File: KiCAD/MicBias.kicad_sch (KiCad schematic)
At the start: 24 parts

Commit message: Added a debug header
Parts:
- renumbered C68 to C62, C69 to C63, C66 to C64, C67 to C65, C64 to C66, C65 to C67, C62 to C68, C63 to C69, R51 to R41, R52 to R42, R49 to R43, R50 to R44, R55 to R45, R56 to R46, R53 to R47, R54 to R48, R43 to R49, R44 to R50, R41 to R51, R42 to R52, R47 to R53, R48 to R54, R45 to R55, R46 to R56
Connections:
- net IN1: now also C62.1; no longer C68.1
- net IN2: now also C63.1; no longer C69.1
- net IN3: now also C64.1; no longer C66.1
- net IN4: now also C65.1; no longer C67.1
- net IN5: now also C66.1; no longer C64.1
- net IN6: now also C67.1; no longer C65.1
- net IN7: now also C68.1; no longer C62.1
- net IN8: now also C69.1; no longer C63.1
- net OUT1: now also C62.2, R41.2, R45.1; no longer C68.2, R51.2, R55.1
- net OUT2: now also C63.2, R42.2, R46.1; no longer C69.2, R52.2, R56.1
- net OUT3: now also C64.2, R43.2, R47.1; no longer C66.2, R49.2, R53.1
- net OUT4: now also C65.2, R44.2, R48.1; no longer C67.2, R50.2, R54.1
- net OUT5: now also C66.2, R49.2, R53.1; no longer C64.2, R43.2, R47.1
- net OUT6: now also C67.2, R50.2, R54.1; no longer C65.2, R44.2, R48.1
- net OUT7: now also C68.2, R51.2, R55.1; no longer C62.2, R41.2, R45.1
- net OUT8: now also C69.2, R52.2, R56.1; no longer C63.2, R42.2, R46.1
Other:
- moved on the sheet: C62, C63, C64, C65, C66, C67, C68, C69, R41, R42, R43, R44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

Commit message: Added PA_Enable pull-down and moved the debug header
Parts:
- renumbered R41 to R42, R42 to R43, R43 to R44, R44 to R45, R45 to R46, R46 to R47, R47 to R48, R48 to R49, R49 to R50, R50 to R51, R51 to R52, R52 to R53, R53 to R54, R54 to R55, R55 to R56, R56 to R57

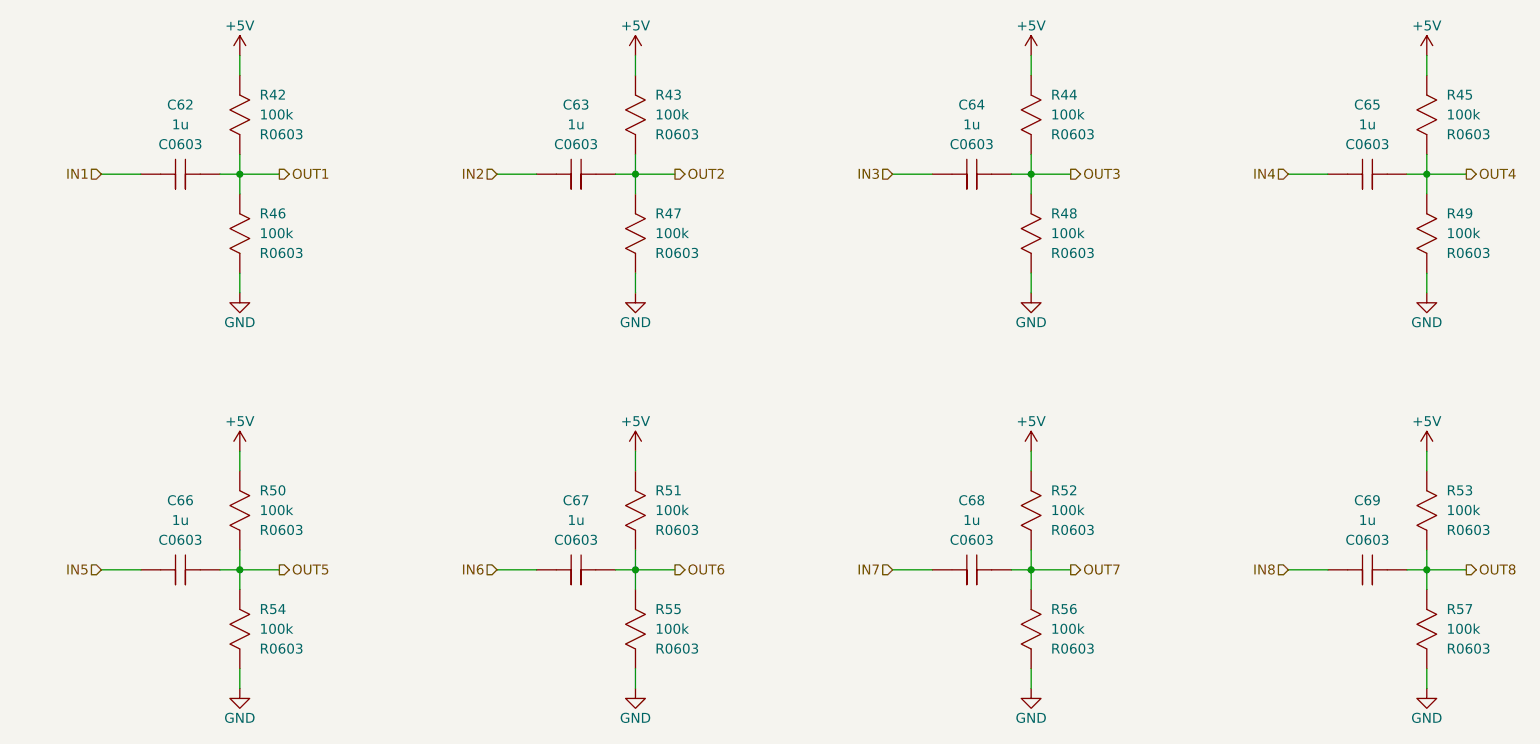
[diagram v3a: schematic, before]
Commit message: Moved the microphone RL to per-channel instead of per-mic
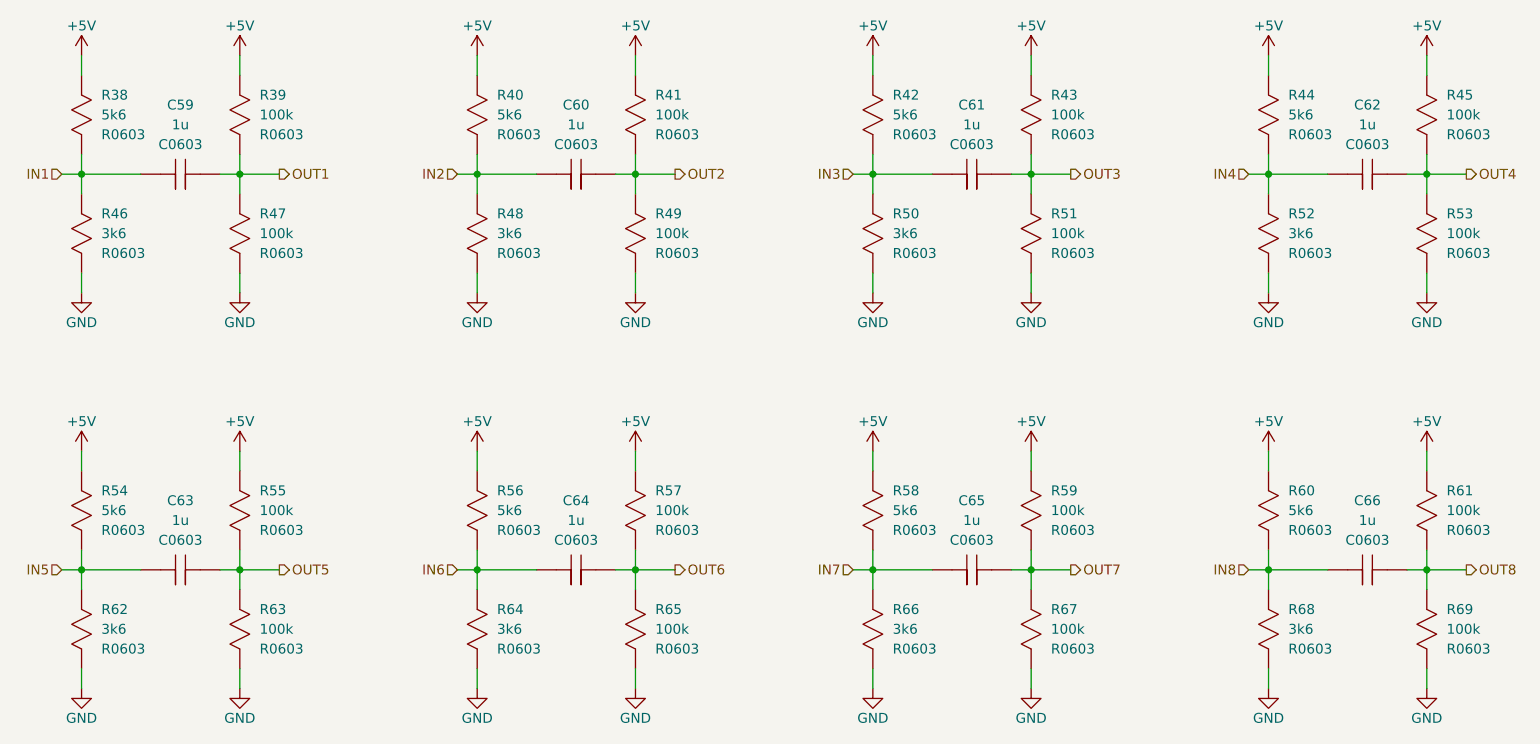
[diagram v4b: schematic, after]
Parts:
- added R38, R40, R42, R44, R54, R56, R58, R60: R0603_5k6, Resistor_SMD:R_0603_1608Metric, symbol Resistors0603:R0603_5k6
- added R46, R48, R50, R52, R62, R64, R66, R68: R0603_3k6, Resistor_SMD:R_0603_1608Metric, symbol Resistors0603:R0603_3k6
- renumbered C62 to C59, C63 to C60, C64 to C61, C65 to C62, C66 to C63, C67 to C64, C68 to C65, C69 to C66, R42 to R39, R43 to R41, R44 to R43, R46 to R47, R47 to R49, R48 to R51, R49 to R53, R50 to R55, R51 to R57, R52 to R59, R53 to R61, R54 to R63, R55 to R65, R56 to R67, R57 to R69
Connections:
- net +5V: now also R38.1, R40.1, R42.1, R44.1, R54.1, R56.1, R58.1, R60.1
- net GND: now also R46.2, R48.2, R50.2, R52.2, R62.2, R64.2, R66.2, R68.2
- net IN1: now also R38.2, R46.1
- net IN2: now also R40.2, R48.1
- net IN3: now also R42.2, R50.1
- net IN4: now also R44.2, R52.1
- net IN5: now also R54.2, R62.1
- net IN6: now also R56.2, R64.1
- net IN7: now also R58.2, R66.1
- net IN8: now also R60.2, R68.1

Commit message: Added title block and version text
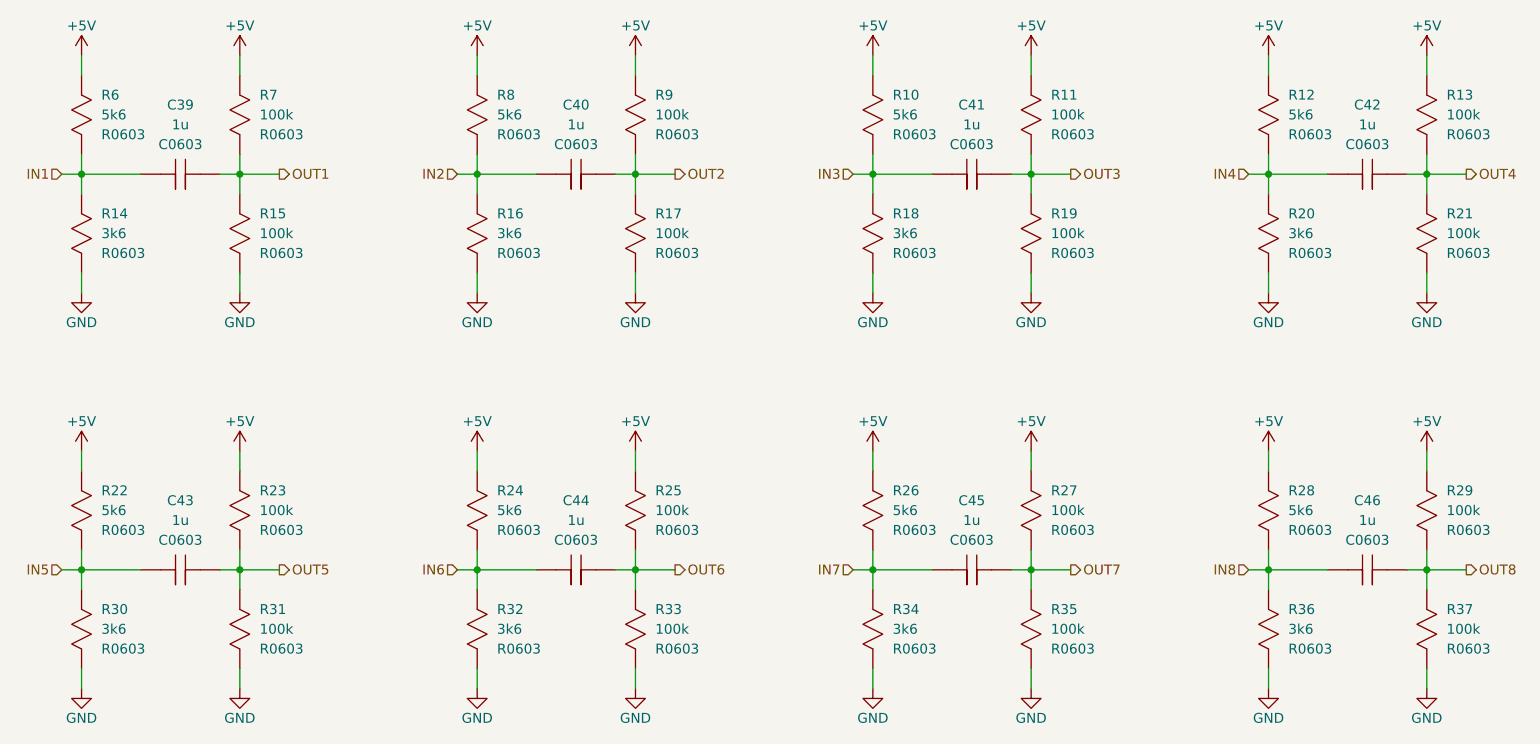
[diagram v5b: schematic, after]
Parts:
- renumbered C59 to C39, C60 to C40, C61 to C41, C62 to C42, C63 to C43, C64 to C44, C65 to C45, C66 to C46, R42 to R10, R43 to R11, R44 to R12, R45 to R13, R46 to R14, R47 to R15, R48 to R16, R49 to R17, R50 to R18, R51 to R19, R52 to R20, R53 to R21, R54 to R22, R55 to R23, R56 to R24, R57 to R25, R58 to R26, R59 to R27, R60 to R28, R61 to R29, R62 to R30, R63 to R31, R64 to R32, R65 to R33, R66 to R34, R67 to R35, R68 to R36, R69 to R37, R38 to R6, R39 to R7, R40 to R8, R41 to R9
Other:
- company: (none) -> University of Cape Town
- title: (none) -> Microphone Biassing

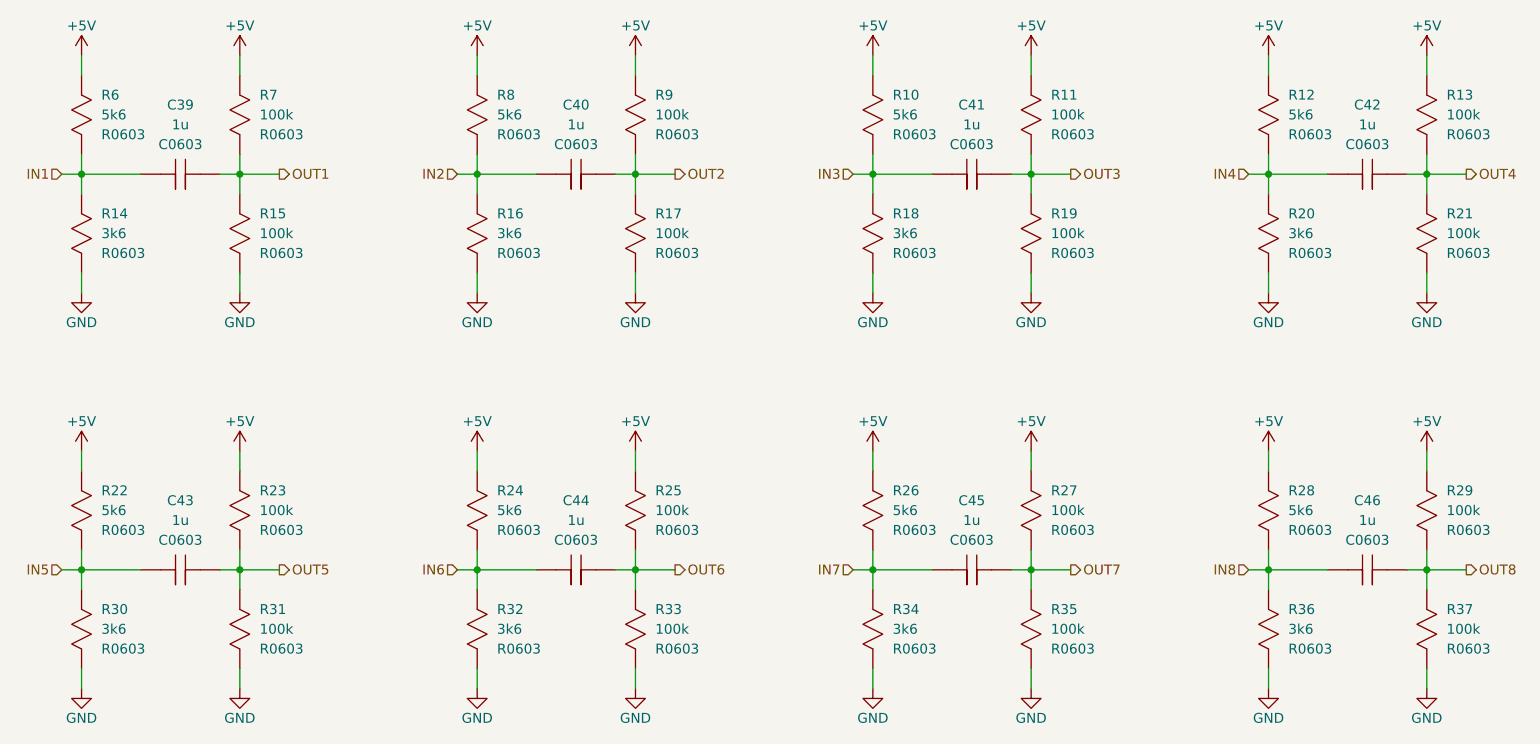
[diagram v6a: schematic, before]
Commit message: Final Updates:
- Mounting holes for an isolation shield
- 5V test-point to inject power
- Test signal input with resistor ladder
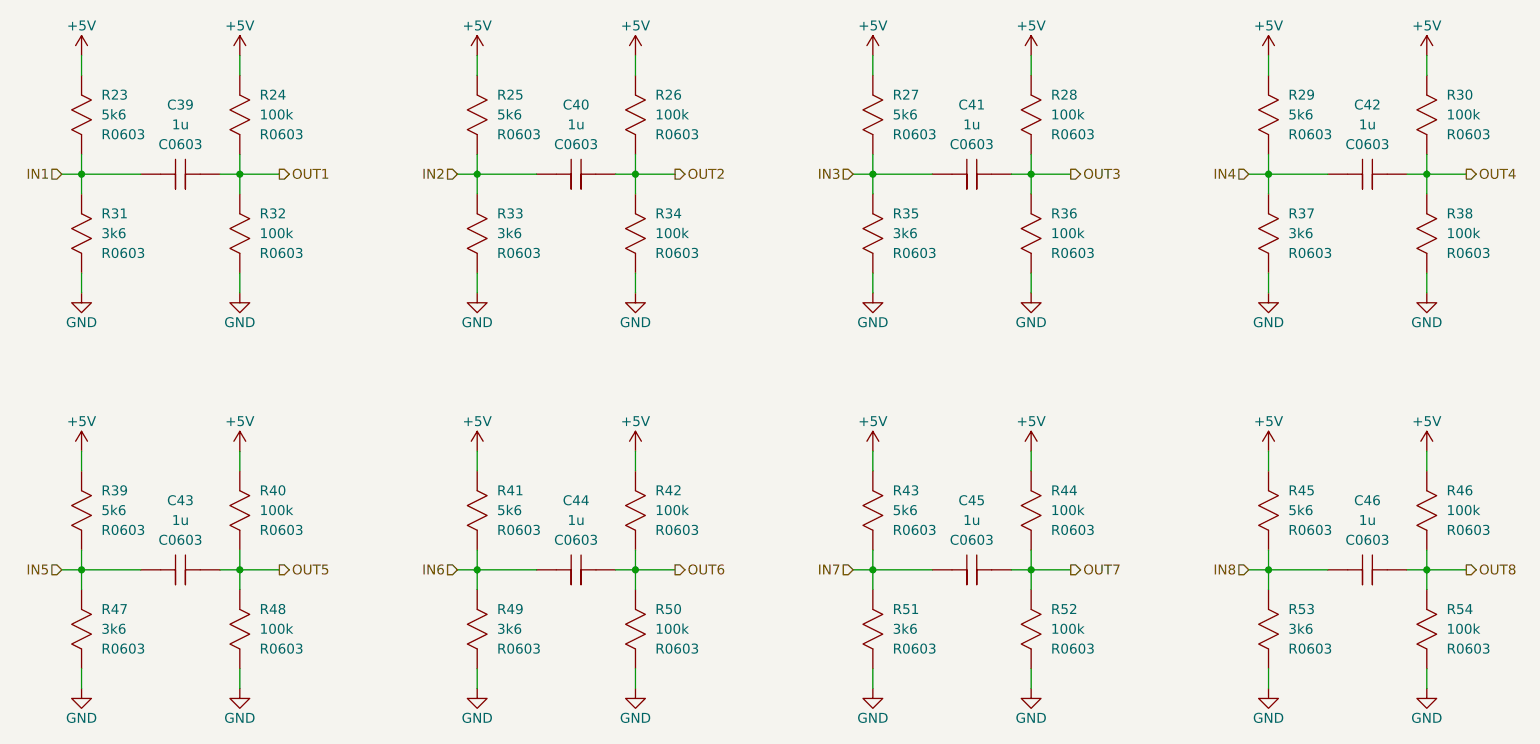
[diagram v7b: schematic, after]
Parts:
- renumbered R6 to R23, R7 to R24, R8 to R25, R9 to R26, R10 to R27, R11 to R28, R12 to R29, R13 to R30, R14 to R31, R15 to R32, R16 to R33, R17 to R34, R18 to R35, R19 to R36, R20 to R37, R21 to R38, R22 to R39, R23 to R40, R24 to R41, R25 to R42, R26 to R43, R27 to R44, R28 to R45, R29 to R46, R30 to R47, R31 to R48, R32 to R49, R33 to R50, R34 to R51, R35 to R52, R36 to R53, R37 to R54
